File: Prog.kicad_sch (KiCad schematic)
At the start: 22 parts, among them J2 JTAG, J3 microUSB, Q1 MMBT3904, Q2 MMBT3904, U12 CH340G, U7 74AHCT573PW, Y1 12M

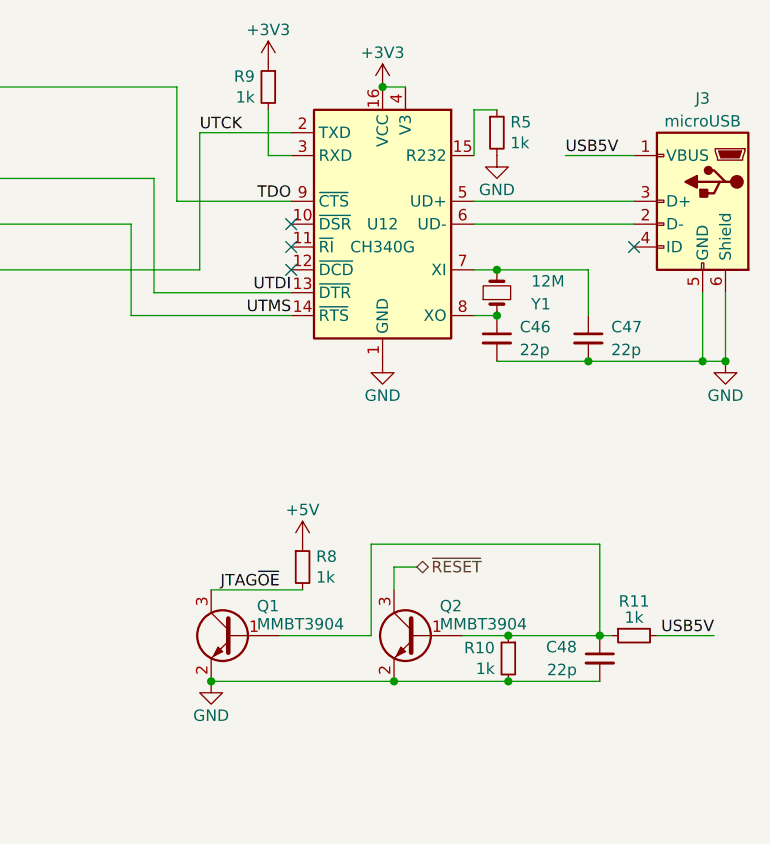
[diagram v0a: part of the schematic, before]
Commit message: Migrate to KiCAD 6
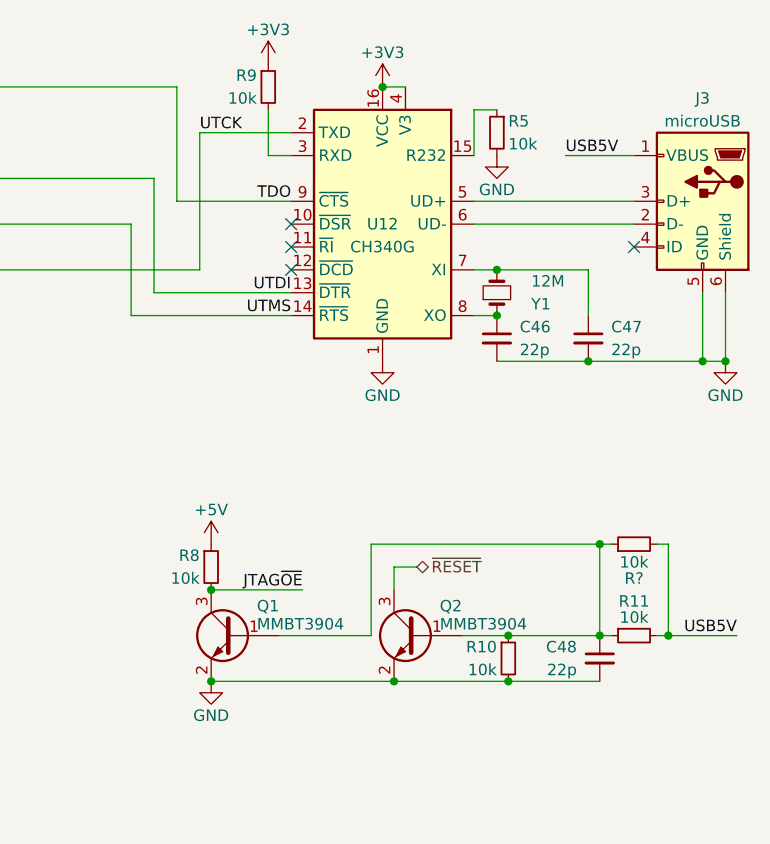
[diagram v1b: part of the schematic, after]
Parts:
- added R?: 10k, stdpads:R_0603, symbol Device:R_Small
- Q1, Q2: LCSC Part (none) -> C20526
- R10, R11, R5, R8, R9: value 1k -> 10k; LCSC Part C21190 -> C25804
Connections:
- net USB5V: now also R?.2
- net at C48.1, Q1.1 (B), Q2.1 (B)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: now also R?.1

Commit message: Documentation update
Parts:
- gave numbers to parts that had none: 1
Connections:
- net at C48.1, Q2.1 (B), R10.1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: no longer Q1.1 (B), R7.1
- new net: Q1.1 (B), R7.1
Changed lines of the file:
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@@
   (junction (at 243.84 74.93) (diameter 0) (color 0 0 0 0)
-  )
-  (junction (at 245.11 95.25) (diameter 0) (color 0 0 0 0)
   )
   (junction (at 252.73 105.41) (diameter 0) (color 0 0 0 0)
@@
   (no_connect (at 139.7 62.23))
   (no_connect (at 139.7 67.31))
-  (wire (pts (xy 245.11 95.25) (xy 246.38 95.25))
+  (wire (pts (xy 219.71 95.25) (xy 246.38 95.25))
     (stroke (width 0) (type default) (color 0 0 0 0))
   )
@@
     (stroke (width 0) (type default) (color 0 0 0 0))
   )
-  (wire (pts (xy 219.71 95.25) (xy 245.11 95.25))
-    (stroke (width 0) (type default) (color 0 0 0 0))
-  )
   (wire (pts (xy 139.7 64.77) (xy 129.54 64.77))
     (stroke (width 0) (type default) (color 0 0 0 0))
@@
   )
   (wire (pts (xy 160.02 64.77) (xy 200.66 64.77))
-    (stroke (width 0) (type default) (color 0 0 0 0))
-  )
-  (wire (pts (xy 245.11 95.25) (xy 245.11 105.41))
     (stroke (width 0) (type default) (color 0 0 0 0))
   )
@@
   (symbol (lib_id "Device:R_Small") (at 248.92 95.25 90) (unit 1)
     (in_bom yes) (on_board yes)
-    (property "Reference" "R?" (id 0) (at 248.92 99.06 90))
+    (property "Reference" "R7" (id 0) (at 248.92 99.06 90))
     (property "Value" "10k" (id 1) (at 248.92 96.52 90)
       (effects (font (size 1.27 1.27)) (justify bottom))

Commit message: idk
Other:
- moved on the sheet: J2, R15, R16

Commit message: Toward final "A"
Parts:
- removed C48: 22p, stdpads:C_0603, symbol Device:C_Small
- removed R7: 10k, stdpads:R_0603, symbol Device:R_Small
- removed U7: 74AHCT573PW, stdpads:TSSOP-20_4.4x6.5mm_P0.65mm, symbol GW_Logic:74573
- added C52: 22p, stdpads:C_0603, symbol Device:C_Small
- added Q3, Q4: MMBT3904, stdpads:SOT-23, symbol Transistor_BJT:MMBT3904
- added R13: 1k, stdpads:R_0603, symbol Device:R_Small
- added R14: 1k5, stdpads:R_0603, symbol Device:R_Small
- added R2: 47, stdpads:R_0603, symbol Device:R_Small
- added U25: 74LVC245APW, stdpads:TSSOP-20_4.4x6.5mm_P0.65mm, symbol GW_Logic:74245
- R10: value 10k -> 470; footprint stdpads:R_0603 -> stdpads:R_0805; LCSC Part C25804 -> (none)
- R11, R8: value 10k -> 1k; LCSC Part C25804 -> (none)
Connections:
- net +3V3: now also U25.20 (Vcc); no longer C23.1, R9.1, U12.16 (VCC), U12.4 (V3)
- net +5V: now also R8.2; no longer C49.1, R8.1
- net GND: now also C52.2, R13.1, U25.1 (AtoB), U25.10 (GND), U25.12 (B6), U25.14 (B4), U25.16 (B2), U25.18 (B0), U25.2 (A0), U25.4 (A2), U25.6 (A4), U25.8 (A6); no longer Q2.2 (E), R10.2
- net JTAG~{OE}: now also R8.1, U25.19 (~{OE}); no longer R8.2
- net TCK: now also C52.1, R2.2
- net TDI: now also U25.3 (A1)
- net TDO: now also U25.11 (B7); no longer U12.9 (~{CTS})
- net TMS: now also U25.5 (A3)
- net USB5V: now also C23.1, R10.1, R9.1, U12.10 (~{DSR}), U12.11 (~{RI}), U12.12 (~{DCD}), U12.16 (VCC), Q4.1 (B), Q4.3 (C)
- net UTCK: now also U25.13 (B5)
- net UTDI: now also U25.17 (B1)
- net UTMS: now also U25.15 (B3)
- net at Q2.1 (B), R11.1: no longer R10.1
- net at Q1.1 (B): now also R13.2, R14.1
- new net: Q2.2 (E), R10.2
- new net: R2.1, U25.7 (A5)
- new net: Q3.2 (E), R14.2
- new net: Q3.1 (B), Q3.3 (C), Q4.2 (E)
- new net CH340G3V3: C49.1, U12.4 (V3)
- new net UTDO: U12.9 (~{CTS}), U25.9 (A7)
- no-connect marks 12 -> 4
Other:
- moved on the sheet: C49, J2, Q1, R10, R15, R16

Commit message: idk
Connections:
- net USB5V: no longer C25.1, R9.1, U12.16 (VCC)
- new net: R9.1, U12.16 (VCC)
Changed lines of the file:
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@@
   (junction (at 156.21 48.26) (diameter 0) (color 0 0 0 0)
   )
-  (junction (at 220.98 41.91) (diameter 0) (color 0 0 0 0)
-  )
   (junction (at 179.07 63.5) (diameter 0) (color 0 0 0 0)
   )
@@
   )
   (junction (at 260.35 146.05) (diameter 0) (color 0 0 0 0)
-  )
-  (junction (at 229.87 140.97) (diameter 0) (color 0 0 0 0)
   )
   (junction (at 219.71 146.05) (diameter 0) (color 0 0 0 0)
@@
     (stroke (width 0) (type default))
   )
-  (wire (pts (xy 229.87 140.97) (xy 240.03 140.97))
-    (stroke (width 0) (type default))
-  )
   (wire (pts (xy 208.28 46.99) (xy 208.28 52.07))
     (stroke (width 0) (type default))
@@
   )
   (wire (pts (xy 224.79 97.79) (xy 222.25 97.79))
-    (stroke (width 0) (type default))
-  )
-  (wire (pts (xy 220.98 41.91) (xy 226.06 41.91))
     (stroke (width 0) (type default))
   )
@@
     )
   )
-  (global_label "USB5V" (shape input) (at 226.06 41.91 0) (fields_autoplaced)
-    (effects (font (size 1.27 1.27)) (justify left))
-    (property "Intersheetrefs" "${INTERSHEET_REFS}" (at 234.4197 41.91 0)
-      (effects (font (size 1.27 1.27)) (justify left) hide)
-    )
-  )

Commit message: Revert "idk"
This reverts commit aa30aa8a559ae1d3e965923a55380a6d00f93ea4.
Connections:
- net USB5V: now also C25.1, R9.1, U12.16 (VCC)
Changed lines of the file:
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@@
   (junction (at 156.21 48.26) (diameter 0) (color 0 0 0 0)
   )
+  (junction (at 220.98 41.91) (diameter 0) (color 0 0 0 0)
+  )
   (junction (at 179.07 63.5) (diameter 0) (color 0 0 0 0)
   )
@@
   )
   (junction (at 260.35 146.05) (diameter 0) (color 0 0 0 0)
+  )
+  (junction (at 229.87 140.97) (diameter 0) (color 0 0 0 0)
   )
   (junction (at 219.71 146.05) (diameter 0) (color 0 0 0 0)
@@
     (stroke (width 0) (type default))
   )
+  (wire (pts (xy 229.87 140.97) (xy 240.03 140.97))
+    (stroke (width 0) (type default))
+  )
   (wire (pts (xy 208.28 46.99) (xy 208.28 52.07))
     (stroke (width 0) (type default))
@@
   )
   (wire (pts (xy 224.79 97.79) (xy 222.25 97.79))
+    (stroke (width 0) (type default))
+  )
+  (wire (pts (xy 220.98 41.91) (xy 226.06 41.91))
     (stroke (width 0) (type default))
   )
@@
     )
   )
+  (global_label "USB5V" (shape input) (at 226.06 41.91 0) (fields_autoplaced)
+    (effects (font (size 1.27 1.27)) (justify left))
+    (property "Intersheetrefs" "${INTERSHEET_REFS}" (at 234.4197 41.91 0)
+      (effects (font (size 1.27 1.27)) (justify left) hide)
+    )
+  )
